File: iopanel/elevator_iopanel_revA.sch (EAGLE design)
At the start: 48 parts, among them U2 TLC6C598-Q1, U3 TLC6C598-Q1, U4 SN74HC165DR, U6 TLC6C598-Q1, X3 MSTBA2

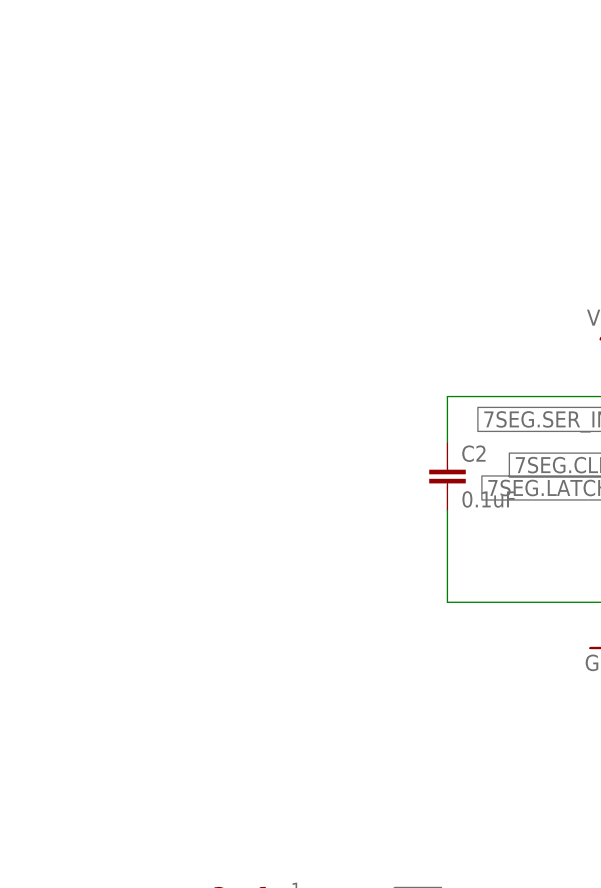
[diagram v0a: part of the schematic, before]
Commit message: Added LEDs for power rails, silkscreen. sent to fab
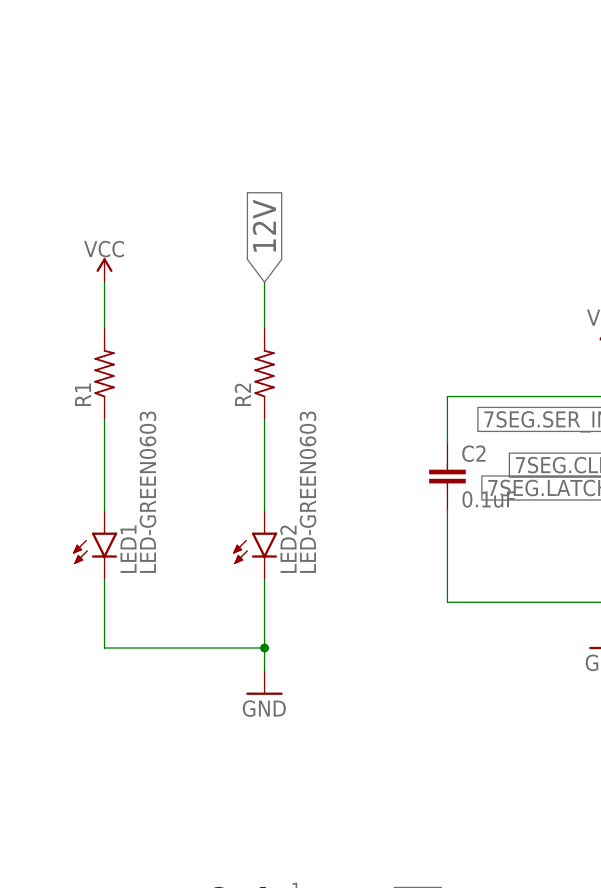
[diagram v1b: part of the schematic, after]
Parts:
- added LED1, LED2: LED-GREEN0603, BeagleBone_Blue_R3:LED-GREEN0603
- added R1, R2: (no value), adafruit:R-US_R0603
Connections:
- new net N$1: LED1.A, R1.1
- new net N$2: LED2.A, R2.1
- net 12V: now also R2.2
- net GND: now also LED1.C, LED2.C
- net VCC: now also R1.2
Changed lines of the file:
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@@
 <part name="GND10" library="SparkFun-Aesthetics" deviceset="GND" device=""/>
 <part name="X3" library="con-phoenix-508" library_urn="urn:adsk.eagle:library:176" deviceset="MSTBA2" device="" package3d_urn="urn:adsk.eagle:package:9615/1"/>
+<part name="LED1" library="BeagleBone_Blue_R3" library_urn="urn:adsk.eagle:library:5828899" deviceset="LED-GREEN" device="0603" package3d_urn="urn:adsk.eagle:package:5829989/8"/>
+<part name="LED2" library="BeagleBone_Blue_R3" library_urn="urn:adsk.eagle:library:5828899" deviceset="LED-GREEN" device="0603" package3d_urn="urn:adsk.eagle:package:5829989/8"/>
+<part name="R1" library="adafruit" library_urn="urn:adsk.eagle:library:420" deviceset="R-US_" device="R0603" package3d_urn="urn:adsk.eagle:package:6240565/1"/>
+<part name="R2" library="adafruit" library_urn="urn:adsk.eagle:library:420" deviceset="R-US_" device="R0603" package3d_urn="urn:adsk.eagle:package:6240565/1"/>
+<part name="GND24" library="SparkFun-Aesthetics" deviceset="GND" device=""/>
+<part name="U$28" library="SparkFun-PowerSymbols" library_urn="urn:adsk.eagle:library:530" deviceset="VCCA" device="" value="VCC"/>
 </parts>
 <sheets>
@@
 <attribute name="VALUE" x="17.78" y="85.09" size="1.778" layer="96"/>
 <attribute name="NAME" x="18.796" y="89.789" size="1.778" layer="95" rot="R180"/>
+</instance>
+<instance part="LED1" gate="G$1" x="7.62" y="134.62" smashed="yes">
+<attribute name="NAME" x="11.176" y="130.048" size="1.778" layer="95" rot="R90"/>
+<attribute name="VALUE" x="13.335" y="130.048" size="1.778" layer="96" rot="R90"/>
+</instance>
+<instance part="LED2" gate="G$1" x="25.4" y="134.62" smashed="yes">
+<attribute name="NAME" x="28.956" y="130.048" size="1.778" layer="95" rot="R90"/>
+<attribute name="VALUE" x="31.115" y="130.048" size="1.778" layer="96" rot="R90"/>
+</instance>
+<instance part="R1" gate="G$1" x="7.62" y="152.4" smashed="yes" rot="R90">
+<attribute name="NAME" x="6.1214" y="148.59" size="1.778" layer="95" rot="R90"/>
+<attribute name="VALUE" x="10.922" y="148.59" size="1.778" layer="96" rot="R90"/>
+</instance>
+<instance part="R2" gate="G$1" x="25.4" y="152.4" smashed="yes" rot="R90">
+<attribute name="NAME" x="23.9014" y="148.59" size="1.778" layer="95" rot="R90"/>
+<attribute name="VALUE" x="28.702" y="148.59" size="1.778" layer="96" rot="R90"/>
+</instance>
+<instance part="GND24" gate="1" x="25.4" y="116.84" smashed="yes">
+<attribute name="VALUE" x="22.86" y="114.3" size="1.778" layer="96"/>
+</instance>
+<instance part="U$28" gate="G$1" x="7.62" y="162.56" smashed="yes">
+<attribute name="VALUE" x="7.62" y="165.354" size="1.778" layer="96" align="bottom-center"/>
 </instance>
 </instances>
@@
 <wire x1="40.64" y1="88.9" x2="40.64" y2="83.82" width="0.1524" layer="91"/>
 </segment>
+<segment>
+<pinref part="LED1" gate="G$1" pin="C"/>
+<wire x1="7.62" y1="129.54" x2="7.62" y2="121.92" width="0.1524" layer="91"/>
+<wire x1="7.62" y1="121.92" x2="25.4" y2="121.92" width="0.1524" layer="91"/>
+<pinref part="GND24" gate="1" pin="GND"/>
+<wire x1="25.4" y1="119.38" x2="25.4" y2="121.92" width="0.1524" layer="91"/>
+<junction x="25.4" y="121.92"/>
+<pinref part="LED2" gate="G$1" pin="C"/>
+<wire x1="25.4" y1="121.92" x2="25.4" y2="129.54" width="0.1524" layer="91"/>
+</segment>
 </net>
 <net name="12V" class="0">
@@
 <wire x1="226.06" y1="195.58" x2="223.52" y2="195.58" width="0.1524" layer="91"/>
 <label x="223.52" y="195.58" size="1.778" layer="95" rot="R180" xref="yes"/>
+</segment>
+<segment>
+<pinref part="R2" gate="G$1" pin="2"/>
+<wire x1="25.4" y1="157.48" x2="25.4" y2="162.56" width="0.1524" layer="91"/>
+<label x="25.4" y="162.56" size="2.54" layer="95" rot="R90" xref="yes"/>
 </segment>
 </net>
@@
 <junction x="132.08" y="53.34"/>
 </segment>
+<segment>
+<pinref part="R1" gate="G$1" pin="2"/>
+<pinref part="U$28" gate="G$1" pin="VCCA"/>
+<wire x1="7.62" y1="157.48" x2="7.62" y2="162.56" width="0.1524" layer="91"/>
+</segment>
 </net>
 <net name="N$17" class="0">
@@
 </segment>
 </net>
+<net name="N$1" class="0">
+<segment>
+<pinref part="LED1" gate="G$1" pin="A"/>
+<pinref part="R1" gate="G$1" pin="1"/>
+<wire x1="7.62" y1="137.16" x2="7.62" y2="147.32" width="0.1524" layer="91"/>
+</segment>
+</net>
+<net name="N$2" class="0">
+<segment>
+<pinref part="LED2" gate="G$1" pin="A"/>
+<pinref part="R2" gate="G$1" pin="1"/>
+<wire x1="25.4" y1="137.16" x2="25.4" y2="147.32" width="0.1524" layer="91"/>
+</segment>
+</net>
